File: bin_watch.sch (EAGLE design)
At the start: 107 parts, among them J1 USB3100-XX-X_REVB, Q1 32.768kHz, T1 2N7002BKV, T2 2N7002BKV, T3 2N7002BKV, T4 2N7002BKV, T5 PMDT670UPE, T6 PMDT670UPE, T7 PMDT670UPE, U1 MCP73831T-2ACI/OT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

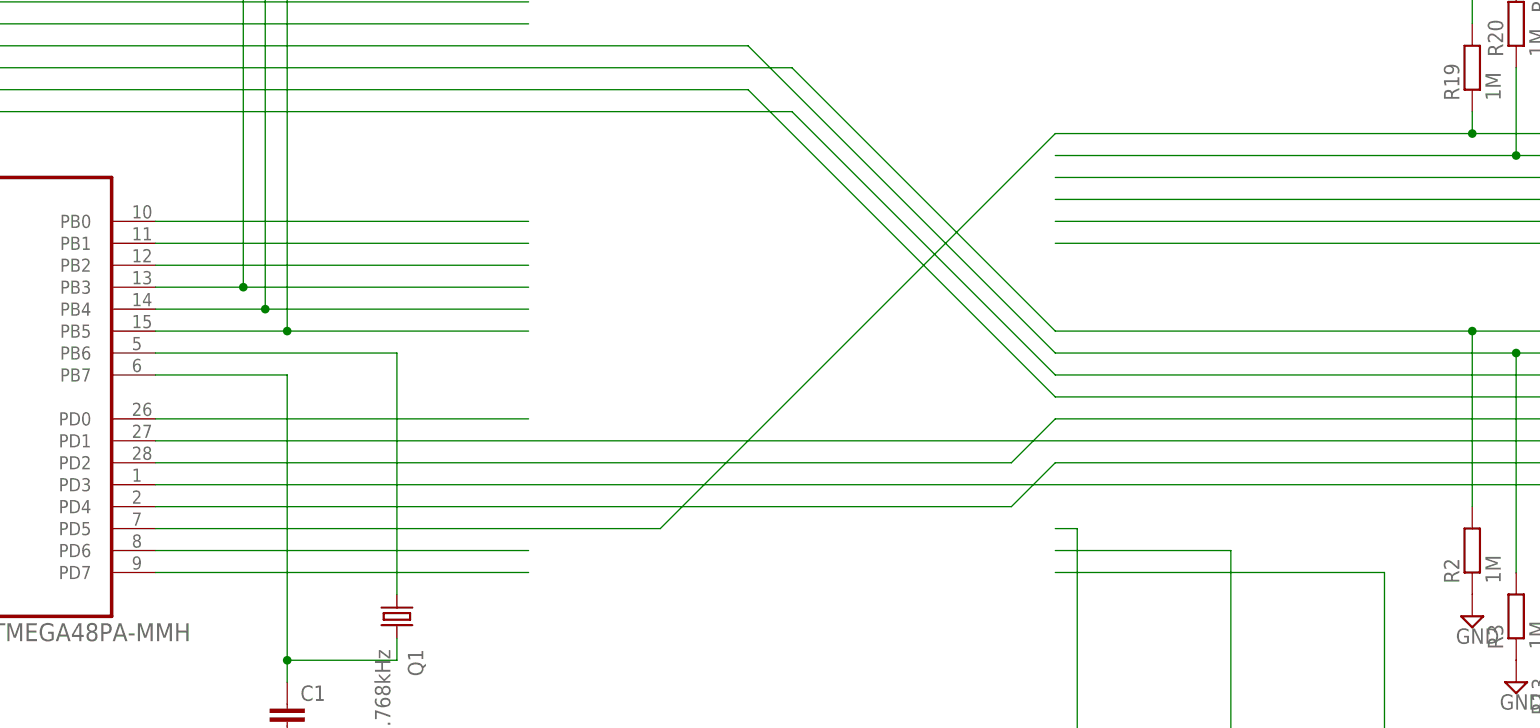
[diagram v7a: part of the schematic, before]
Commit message: New chip wired to IO
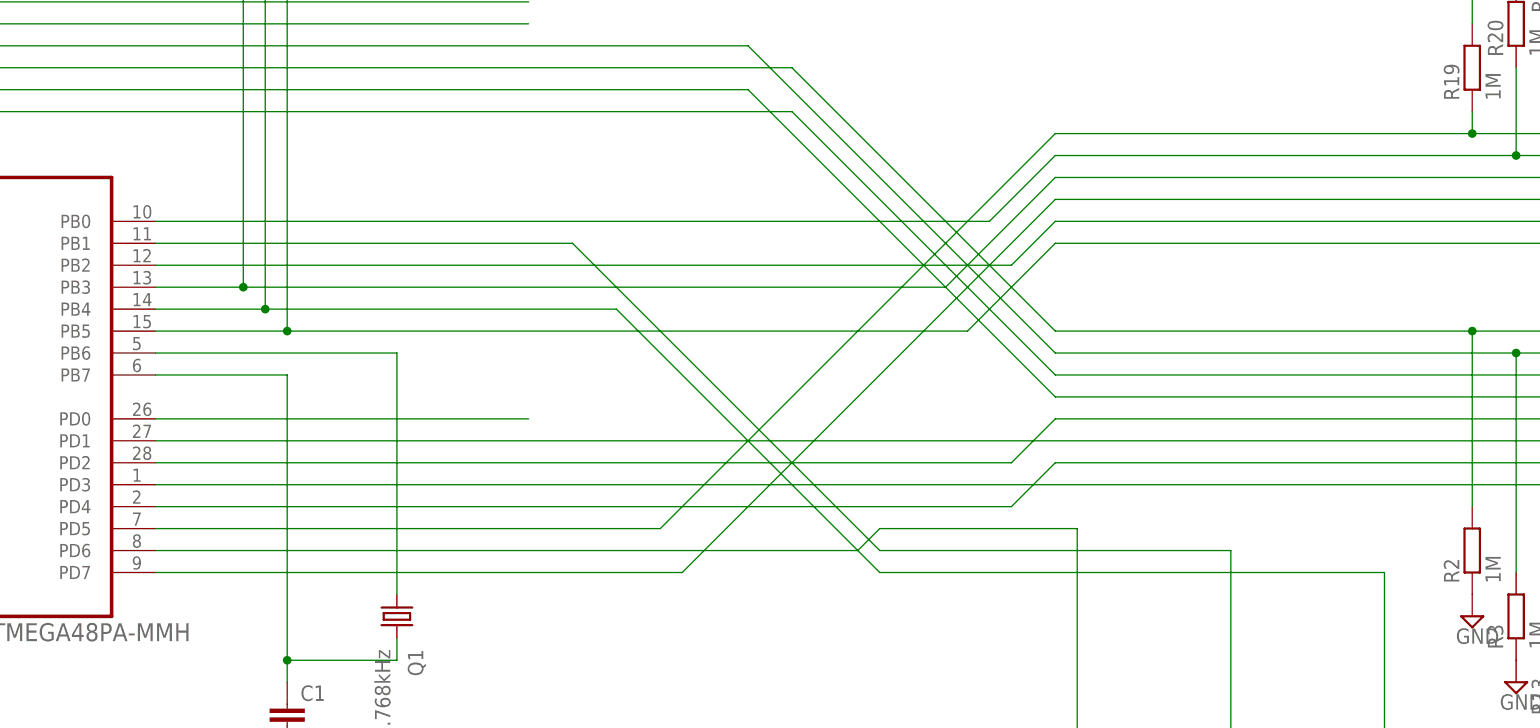
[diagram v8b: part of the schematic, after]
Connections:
- removed net N$12: U4.PB0
- removed net N$13: U4.PB1
- removed net N$14: U4.PB2
- removed net N$2: U4.PB3
- removed net N$21: U4.PD6
- removed net N$22: U4.PD7
- removed net N$4: U4.PB4
- removed net N$5: U4.PB5
- net BTN1: now also U4.PD6
- net BTN2: now also U4.PB1
- net BTN3: now also U4.PB4
- net G_BLOCK1: now also U4.PB0
- net G_BLOCK2: now also U4.PB3
- net G_BLOCK3: now also U4.PD7
- net G_BLOCK4: now also U4.PB2
- net G_BLOCK5: now also U4.PB5
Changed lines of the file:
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@@
 <wire x1="91.44" y1="15.24" x2="91.44" y2="12.7" width="0.1524" layer="91"/>
 <junction x="91.44" y="15.24"/>
-<wire x1="88.9" y1="48.26" x2="91.44" y2="48.26" width="0.1524" layer="91"/>
+<wire x1="68.58" y1="48.26" x2="91.44" y2="48.26" width="0.1524" layer="91"/>
+<pinref part="U4" gate="A" pin="PD6"/>
+<wire x1="-15.24" y1="45.72" x2="66.04" y2="45.72" width="0.1524" layer="91"/>
+<wire x1="68.58" y1="48.26" x2="66.04" y2="45.72" width="0.1524" layer="91"/>
 </segment>
 </net>
@@
 <wire x1="109.22" y1="15.24" x2="109.22" y2="12.7" width="0.1524" layer="91"/>
 <junction x="109.22" y="15.24"/>
-<wire x1="88.9" y1="45.72" x2="109.22" y2="45.72" width="0.1524" layer="91"/>
+<wire x1="68.58" y1="45.72" x2="109.22" y2="45.72" width="0.1524" layer="91"/>
+<pinref part="U4" gate="A" pin="PB1"/>
+<wire x1="-15.24" y1="81.28" x2="33.02" y2="81.28" width="0.1524" layer="91"/>
+<wire x1="68.58" y1="45.72" x2="33.02" y2="81.28" width="0.1524" layer="91"/>
 </segment>
 </net>
@@
 <wire x1="127" y1="15.24" x2="127" y2="12.7" width="0.1524" layer="91"/>
 <junction x="127" y="15.24"/>
-<wire x1="88.9" y1="43.18" x2="127" y2="43.18" width="0.1524" layer="91"/>
+<wire x1="68.58" y1="43.18" x2="127" y2="43.18" width="0.1524" layer="91"/>
+<pinref part="U4" gate="A" pin="PB4"/>
+<wire x1="-15.24" y1="73.66" x2="-2.54" y2="73.66" width="0.1524" layer="91"/>
+<wire x1="-2.54" y1="73.66" x2="38.1" y2="73.66" width="0.1524" layer="91"/>
+<junction x="-2.54" y="73.66"/>
+<wire x1="-2.54" y1="73.66" x2="-2.54" y2="119.38" width="0.1524" layer="91"/>
+<wire x1="-2.54" y1="119.38" x2="-101.6" y2="119.38" width="0.1524" layer="91"/>
+<wire x1="68.58" y1="43.18" x2="38.1" y2="73.66" width="0.1524" layer="91"/>
 </segment>
 </net>
@@
 <wire x1="142.24" y1="101.6" x2="142.24" y2="91.44" width="0.1524" layer="91"/>
 <junction x="142.24" y="91.44"/>
+<pinref part="U4" gate="A" pin="PB0"/>
+<wire x1="88.9" y1="91.44" x2="81.28" y2="83.82" width="0.1524" layer="91"/>
+<wire x1="81.28" y1="83.82" x2="-15.24" y2="83.82" width="0.1524" layer="91"/>
 </segment>
 </net>
@@
 <wire x1="147.32" y1="106.68" x2="147.32" y2="88.9" width="0.1524" layer="91"/>
 <junction x="147.32" y="88.9"/>
+<pinref part="U4" gate="A" pin="PB3"/>
+<wire x1="-15.24" y1="76.2" x2="-5.08" y2="76.2" width="0.1524" layer="91"/>
+<junction x="-5.08" y="76.2"/>
+<wire x1="-5.08" y1="76.2" x2="-5.08" y2="116.84" width="0.1524" layer="91"/>
+<wire x1="-5.08" y1="116.84" x2="-101.6" y2="116.84" width="0.1524" layer="91"/>
+<wire x1="88.9" y1="88.9" x2="76.2" y2="76.2" width="0.1524" layer="91"/>
+<wire x1="76.2" y1="76.2" x2="-5.08" y2="76.2" width="0.1524" layer="91"/>
 </segment>
 </net>
@@
 <wire x1="152.4" y1="96.52" x2="152.4" y2="86.36" width="0.1524" layer="91"/>
 <junction x="152.4" y="86.36"/>
+<pinref part="U4" gate="A" pin="PD7"/>
+<wire x1="-15.24" y1="43.18" x2="45.72" y2="43.18" width="0.1524" layer="91"/>
+<wire x1="88.9" y1="86.36" x2="45.72" y2="43.18" width="0.1524" layer="91"/>
 </segment>
 </net>
@@
 <wire x1="157.48" y1="101.6" x2="157.48" y2="83.82" width="0.1524" layer="91"/>
 <junction x="157.48" y="83.82"/>
+<pinref part="U4" gate="A" pin="PB2"/>
+<wire x1="88.9" y1="83.82" x2="83.82" y2="78.74" width="0.1524" layer="91"/>
+<wire x1="83.82" y1="78.74" x2="-15.24" y2="78.74" width="0.1524" layer="91"/>
 </segment>
 </net>
@@
 <wire x1="162.56" y1="106.68" x2="162.56" y2="81.28" width="0.1524" layer="91"/>
 <junction x="162.56" y="81.28"/>
+<pinref part="U4" gate="A" pin="PB5"/>
+<wire x1="-15.24" y1="71.12" x2="0" y2="71.12" width="0.1524" layer="91"/>
+<junction x="0" y="71.12"/>
+<wire x1="0" y1="71.12" x2="0" y2="121.92" width="0.1524" layer="91"/>
+<wire x1="0" y1="121.92" x2="-101.6" y2="121.92" width="0.1524" layer="91"/>
+<wire x1="88.9" y1="81.28" x2="78.74" y2="71.12" width="0.1524" layer="91"/>
+<wire x1="78.74" y1="71.12" x2="0" y2="71.12" width="0.1524" layer="91"/>
 </segment>
 </net>
@@
 </segment>
 </net>
-<net name="N$2" class="0">
-<segment>
-<pinref part="U4" gate="A" pin="PB3"/>
-<wire x1="-15.24" y1="76.2" x2="-5.08" y2="76.2" width="0.1524" layer="91"/>
-<wire x1="-5.08" y1="76.2" x2="27.94" y2="76.2" width="0.1524" layer="91"/>
-<junction x="-5.08" y="76.2"/>
-<wire x1="-5.08" y1="76.2" x2="-5.08" y2="116.84" width="0.1524" layer="91"/>
-<wire x1="-5.08" y1="116.84" x2="-101.6" y2="116.84" width="0.1524" layer="91"/>
-</segment>
-</net>
-<net name="N$4" class="0">
-<segment>
-<pinref part="U4" gate="A" pin="PB4"/>
-<wire x1="-15.24" y1="73.66" x2="-2.54" y2="73.66" width="0.1524" layer="91"/>
-<wire x1="-2.54" y1="73.66" x2="27.94" y2="73.66" width="0.1524" layer="91"/>
-<junction x="-2.54" y="73.66"/>
-<wire x1="-2.54" y1="73.66" x2="-2.54" y2="119.38" width="0.1524" layer="91"/>
-<wire x1="-2.54" y1="119.38" x2="-101.6" y2="119.38" width="0.1524" layer="91"/>
-</segment>
-</net>
-<net name="N$5" class="0">
-<segment>
-<pinref part="U4" gate="A" pin="PB5"/>
-<wire x1="-15.24" y1="71.12" x2="0" y2="71.12" width="0.1524" layer="91"/>
-<wire x1="0" y1="71.12" x2="27.94" y2="71.12" width="0.1524" layer="91"/>
-<junction x="0" y="71.12"/>
-<wire x1="0" y1="71.12" x2="0" y2="121.92" width="0.1524" layer="91"/>
-<wire x1="0" y1="121.92" x2="-101.6" y2="121.92" width="0.1524" layer="91"/>
-</segment>
-</net>
 <net name="N$10" class="0">
 <segment>
@@
 </segment>
 </net>
-<net name="N$12" class="0">
-<segment>
-<pinref part="U4" gate="A" pin="PB0"/>
-<wire x1="-15.24" y1="83.82" x2="27.94" y2="83.82" width="0.1524" layer="91"/>
-</segment>
-</net>
-<net name="N$13" class="0">
-<segment>
-<pinref part="U4" gate="A" pin="PB1"/>
-<wire x1="-15.24" y1="81.28" x2="27.94" y2="81.28" width="0.1524" layer="91"/>
-</segment>
-</net>
-<net name="N$14" class="0">
-<segment>
-<pinref part="U4" gate="A" pin="PB2"/>
-<wire x1="-15.24" y1="78.74" x2="27.94" y2="78.74" width="0.1524" layer="91"/>
-</segment>
-</net>
 <net name="N$15" class="0">
 <segment>
@@
 </segment>
 </net>
-<net name="N$21" class="0">
-<segment>
-<pinref part="U4" gate="A" pin="PD6"/>
-<wire x1="-15.24" y1="45.72" x2="27.94" y2="45.72" width="0.1524" layer="91"/>
-</segment>
-</net>
-<net name="N$22" class="0">
-<segment>
-<pinref part="U4" gate="A" pin="PD7"/>
-<wire x1="-15.24" y1="43.18" x2="27.94" y2="43.18" width="0.1524" layer="91"/>
-</segment>
-</net>
